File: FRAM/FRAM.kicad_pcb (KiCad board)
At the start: 2 copper layers, 50 x 31 mm, 8 parts, among them IC1 MB85RC256VPF-G-JNERE2, IC2 MB85RC256VPF-G-JNERE2, IC3 MB85RC256VPF-G-JNERE2, IC4 MB85RC256VPF-G-JNERE2

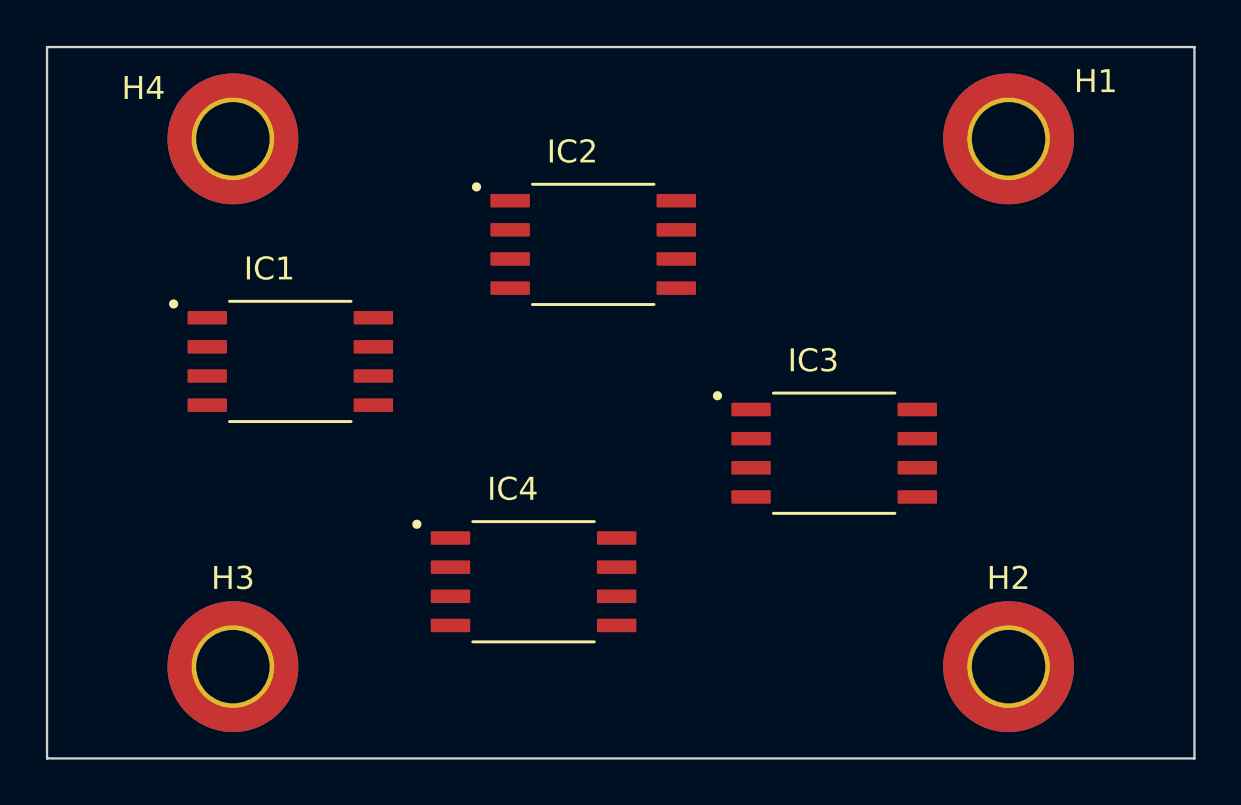
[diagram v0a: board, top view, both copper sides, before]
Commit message: Route sensors, IMU and radio board
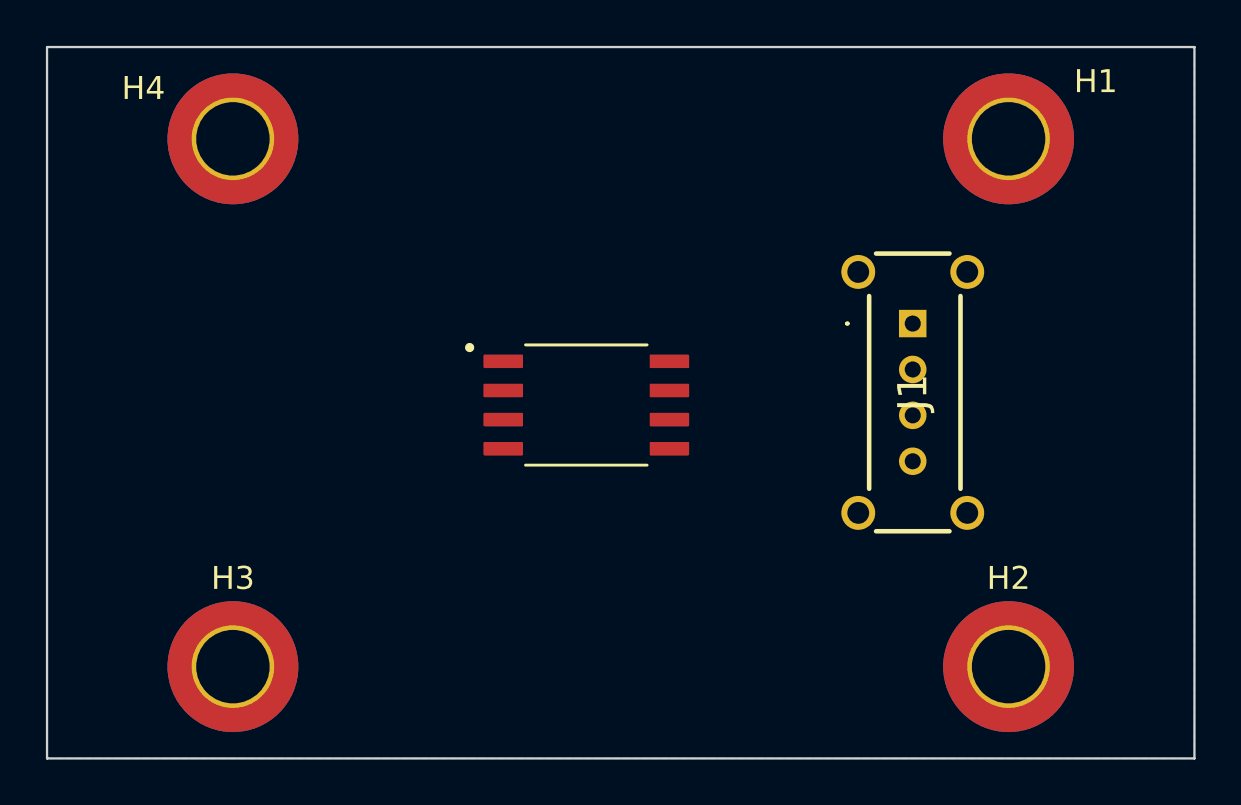
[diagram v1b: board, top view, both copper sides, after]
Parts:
- removed IC2, IC3, IC4: MB85RC256VPF-G-JNERE2, MB85RC256VPF-G-JNERE2:SOP127P797X210-8N
- added J1: M80-8770405, KiCad:M808770405, F.Cu at (135.7, 89.8)
- moved IC1 13.0 mm to (121.5, 93.4)
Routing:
- added copper zone on B.Cu, net GND

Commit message: Done with most of the boards
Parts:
- added R1: R, Resistor_SMD:R_0603_1608Metric, F.Cu at (127.7, 84.1)
- added R2: R, Resistor_SMD:R_0603_1608Metric, F.Cu at (127.7, 86.6)
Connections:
- J1 pad 2: unconnected-(J1-Pad2) -> GND
- J1 pad 3: +3V3 -> /SCL
- J1 pad 4: +3V3 -> /SDA
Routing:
- net +3V3: track 0.00 -> 11.3 mm
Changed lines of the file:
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@@
   (net 5 "+3V3")
   (net 6 "/WP")
-  (net 7 "unconnected-(J1-Pad2)")
-  (net 8 "unconnected-(J1-PadMH1)")
-  (net 9 "unconnected-(J1-PadMH2)")
-  (net 10 "unconnected-(J1-PadMH3)")
-  (net 11 "unconnected-(J1-PadMH4)")
+  (net 7 "unconnected-(J1-PadMH1)")
+  (net 8 "unconnected-(J1-PadMH2)")
+  (net 9 "unconnected-(J1-PadMH3)")
+  (net 10 "unconnected-(J1-PadMH4)")
+  (net 11 "/SCL")
+  (net 12 "/SDA")
+  (net 13 "Net-(IC2-SCL)")
+  (footprint "Resistor_SMD:R_0603_1608Metric" (layer "F.Cu")
+    (at 127.675 86.6)
+    (descr "Resistor SMD 0603 (1608 Metric), square (rectangular) end terminal, IPC_7351 nominal, (Body size source: IPC-SM-782 page 72, https://www.pcb-3d.com/wordpress/wp-content/uploads/ipc-sm-782a_amendment_1_and_2.pdf), generated with kicad-footprint-generator")
+    (tags "resistor")
+    (property "Sheetfile" "FRAM.kicad_sch")
+    (property "Sheetname" "")
+    (property "ki_description" "Resistor")
+    (property "ki_keywords" "R res resistor")
+    (attr smd)
+    (fp_text reference "R2" (at 0 -1.43) (layer "F.SilkS")
+        (effects (font (size 1 1) (thickness 0.15)))
+    )
+    (fp_text value "R" (at 0 1.43) (layer "F.Fab")
+        (effects (font (size 1 1) (thickness 0.15)))
+    )
+    (fp_text user "${REFERENCE}" (at 0 0) (layer "F.Fab")
+        (effects (font (size 0.4 0.4) (thickness 0.06)))
+    )
+    (fp_line (start -0.237258 -0.5225) (end 0.237258 -0.5225)
+      (stroke (width 0.12) (type solid)) (layer "F.SilkS"))
+    (fp_line (start -0.237258 0.5225) (end 0.237258 0.5225)
+      (stroke (width 0.12) (type solid)) (layer "F.SilkS"))
+    (fp_line (start -1.48 -0.73) (end 1.48 -0.73)
+      (stroke (width 0.05) (type solid)) (layer "F.CrtYd"))
+    (fp_line (start -1.48 0.73) (end -1.48 -0.73)
+      (stroke (width 0.05) (type solid)) (layer "F.CrtYd"))
+    (fp_line (start 1.48 -0.73) (end 1.48 0.73)
+      (stroke (width 0.05) (type solid)) (layer "F.CrtYd"))
+    (fp_line (start 1.48 0.73) (end -1.48 0.73)
+      (stroke (width 0.05) (type solid)) (layer "F.CrtYd"))
+    (fp_line (start -0.8 -0.4125) (end 0.8 -0.4125)
+      (stroke (width 0.1) (type solid)) (layer "F.Fab"))
+    (fp_line (start -0.8 0.4125) (end -0.8 -0.4125)
+      (stroke (width 0.1) (type solid)) (layer "F.Fab"))
+    (fp_line (start 0.8 -0.4125) (end 0.8 0.4125)
+      (stroke (width 0.1) (type solid)) (layer "F.Fab"))
+    (fp_line (start 0.8 0.4125) (end -0.8 0.4125)
+      (stroke (width 0.1) (type solid)) (layer "F.Fab"))
+    (pad "1" smd roundrect (at -0.825 0) (size 0.8 0.95) (layers "F.Cu" "F.Paste" "F.Mask") (roundrect_rratio 0.25)
+      (net 12 "/SDA") (pintype "passive"))
+    (pad "2" smd roundrect (at 0.825 0) (size 0.8 0.95) (layers "F.Cu" "F.Paste" "F.Mask") (roundrect_rratio 0.25)
+      (net 12 "/SDA") (pintype "passive"))
+    (model "${KICAD6_3DMODEL_DIR}/Resistor_SMD.3dshapes/R_0603_1608Metric.wrl"
+      (offset (xyz 0 0 0))
+      (scale (xyz 1 1 1))
+      (rotate (xyz 0 0 0))
+    )
+  )
+  (footprint "Resistor_SMD:R_0603_1608Metric" (layer "F.Cu")
+    (at 127.675 84.09)
+    (descr "Resistor SMD 0603 (1608 Metric), square (rectangular) end terminal, IPC_7351 nominal, (Body size source: IPC-SM-782 page 72, https://www.pcb-3d.com/wordpress/wp-content/uploads/ipc-sm-782a_amendment_1_and_2.pdf), generated with kicad-footprint-generator")
+    (tags "resistor")
+    (property "Sheetfile" "FRAM.kicad_sch")
+    (property "Sheetname" "")
+    (property "ki_description" "Resistor")
+    (property "ki_keywords" "R res resistor")
+    (attr smd)
+    (fp_text reference "R1" (at 0 -1.43) (layer "F.SilkS")
+        (effects (font (size 1 1) (thickness 0.15)))
+    )
+    (fp_text value "R" (at 0 1.43) (layer "F.Fab")
+        (effects (font (size 1 1) (thickness 0.15)))
+    )
+    (fp_text user "${REFERENCE}" (at 0 0) (layer "F.Fab")
+        (effects (font (size 0.4 0.4) (thickness 0.06)))
+    )
+    (fp_line (start -0.237258 -0.5225) (end 0.237258 -0.5225)
+      (stroke (width 0.12) (type solid)) (layer "F.SilkS"))
+    (fp_line (start -0.237258 0.5225) (end 0.237258 0.5225)
+      (stroke (width 0.12) (type solid)) (layer "F.SilkS"))
+    (fp_line (start -1.48 -0.73) (end 1.48 -0.73)
+      (stroke (width 0.05) (type solid)) (layer "F.CrtYd"))
+    (fp_line (start -1.48 0.73) (end -1.48 -0.73)
+      (stroke (width 0.05) (type solid)) (layer "F.CrtYd"))
+    (fp_line (start 1.48 -0.73) (end 1.48 0.73)
+      (stroke (width 0.05) (type solid)) (layer "F.CrtYd"))
+    (fp_line (start 1.48 0.73) (end -1.48 0.73)
+      (stroke (width 0.05) (type solid)) (layer "F.CrtYd"))
+    (fp_line (start -0.8 -0.4125) (end 0.8 -0.4125)
+      (stroke (width 0.1) (type solid)) (layer "F.Fab"))
+    (fp_line (start -0.8 0.4125) (end -0.8 -0.4125)
+      (stroke (width 0.1) (type solid)) (layer "F.Fab"))
+    (fp_line (start 0.8 -0.4125) (end 0.8 0.4125)
+      (stroke (width 0.1) (type solid)) (layer "F.Fab"))
+    (fp_line (start 0.8 0.4125) (end -0.8 0.4125)
+      (stroke (width 0.1) (type solid)) (layer "F.Fab"))
+    (pad "1" smd roundrect (at -0.825 0) (size 0.8 0.95) (layers "F.Cu" "F.Paste" "F.Mask") (roundrect_rratio 0.25)
+      (net 13 "Net-(IC2-SCL)") (pintype "passive"))
+    (pad "2" smd roundrect (at 0.825 0) (size 0.8 0.95) (layers "F.Cu" "F.Paste" "F.Mask") (roundrect_rratio 0.25)
+      (net 11 "/SCL") (pintype "passive"))
+    (model "${KICAD6_3DMODEL_DIR}/Resistor_SMD.3dshapes/R_0603_1608Metric.wrl"
+      (offset (xyz 0 0 0))
+      (scale (xyz 1 1 1))
+      (rotate (xyz 0 0 0))
+    )
+  )
   (footprint "MountingHole:MountingHole_3.2mm_M3_ISO7380_Pad_TopBottom" (layer "F.Cu")
     (at 106.1 104.8)
@@
       (net 5 "+3V3") (pinfunction "1") (pintype "passive"))
     (pad "2" thru_hole circle (at -2 0 90) (size 1.2 1.2) (drill 0.7) (layers "*.Cu" "*.Mask")
-      (net 7 "unconnected-(J1-Pad2)") (pinfunction "2") (pintype "passive"))
+      (net 4 "GND") (pinfunction "2") (pintype "passive"))
     (pad "3" thru_hole circle (at -4 0 90) (size 1.2 1.2) (drill 0.7) (layers "*.Cu" "*.Mask")
-      (net 5 "+3V3") (pinfunction "3") (pintype "passive"))
+      (net 11 "/SCL") (pinfunction "3") (pintype "passive"))
     (pad "4" thru_hole circle (at -6 0 90) (size 1.2 1.2) (drill 0.7) (layers "*.Cu" "*.Mask")
-      (net 5 "+3V3") (pinfunction "4") (pintype "passive"))
+      (net 12 "/SDA") (pinfunction "4") (pintype "passive"))
     (pad "MH1" thru_hole circle (at 2.25 -2.375 90) (size 1.478 1.478) (drill 0.95) (layers "*.Cu" "*.Mask")
-      (net 8 "unconnected-(J1-PadMH1)") (pinfunction "MH1") (pintype "passive"))
+      (net 7 "unconnected-(J1-PadMH1)") (pinfunction "MH1") (pintype "passive+no_connect"))
     (pad "MH2" thru_hole circle (at 2.25 2.375 90) (size 1.478 1.478) (drill 0.95) (layers "*.Cu" "*.Mask")
-      (net 9 "unconnected-(J1-PadMH2)") (pinfunction "MH2") (pintype "passive"))
+      (net 8 "unconnected-(J1-PadMH2)") (pinfunction "MH2") (pintype "passive+no_connect"))
     (pad "MH3" thru_hole circle (at -8.25 2.375 90) (size 1.478 1.478) (drill 0.95) (layers "*.Cu" "*.Mask")
-      (net 10 "unconnected-(J1-PadMH3)") (pinfunction "MH3") (pintype "passive"))
+      (net 9 "unconnected-(J1-PadMH3)") (pinfunction "MH3") (pintype "passive+no_connect"))
     (pad "MH4" thru_hole circle (at -8.25 -2.375 90) (size 1.478 1.478) (drill 0.95) (layers "*.Cu" "*.Mask")
-      (net 11 "unconnected-(J1-PadMH4)") (pinfunction "MH4") (pintype "passive"))
+      (net 10 "unconnected-(J1-PadMH4)") (pinfunction "MH4") (pintype "passive+no_connect"))
     (model "M80-8770405.stp"
       (offset (xyz 0 0 0))
@@
   (gr_line (start 98 77.8) (end 98 108.8)
     (stroke (width 0.1) (type default)) (layer "Edge.Cuts"))
+  (segment (start 125.12 91.495) (end 126.765 89.85) (width 0.25) (layer "F.Cu") (net 5))
+  (segment (start 126.765 89.85) (end 135.725 89.85) (width 0.25) (layer "F.Cu") (net 5))
   (zone (net 4) (net_name "GND") (layer "B.Cu") (hatch edge 0.5)
     (connect_pads (clearance 0.5))

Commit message: LC24 PCBs
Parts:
- removed IC1: MB85RC256VPF-G-JNERE2, MB85RC256VPF-G-JNERE2:SOP127P797X210-8N
- removed J1: M80-8770405, KiCad:M808770405
- added IC2: MB85RC256VPF-G-JNERE2, FRAM:FPT-8P-M08_FUJ, F.Cu at (115.0, 92.5)
- added J2: M80-8770422, Harwin-M80-8770422:CONN_M80-87704_HRW, F.Cu at (132.5, 89.8)
- added JP1: SolderJumper_2_Open, Jumper:SolderJumper-2_P1.3mm_Open_RoundedPad1.0x1.5mm, F.Cu at (103.8, 89.0)
- added JP2: SolderJumper_2_Open, Jumper:SolderJumper-2_P1.3mm_Open_RoundedPad1.0x1.5mm, F.Cu at (103.8, 93.0)
- added JP3: SolderJumper_2_Open, Jumper:SolderJumper-2_P1.3mm_Open_RoundedPad1.0x1.5mm, F.Cu at (103.8, 97.0)
- H1, H2, H3, H4: footprint MountingHole:MountingHole_3.2mm_M3_ISO7380_Pad_TopBottom -> Mounting_Wuerth:Mounting_Wuerth_WA-SMSI-M1.6_H1mm_9774010633
- R1, R2: value R -> 10k; footprint Resistor_SMD:R_0603_1608Metric -> Resistor_SMD:R_0201_0603Metric_Pad0.64x0.40mm_HandSolder
- moved R1 11.0 mm to (124.0, 94.5), turned to 90 degrees
- moved R2 6.53 mm to (124.0, 92.0), turned to -90 degrees
- moved H3 4.51 mm to (101.9, 103.1)
- moved H4 4.35 mm to (101.9, 83.1)
- moved H2 2.68 mm to (141.9, 103.1)
- moved H1 2.40 mm to (141.9, 83.1)
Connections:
- H1 pad 1: (no net) -> GND
- H2 pad 1: (no net) -> GND
- H3 pad 1: (no net) -> GND
- H4 pad 1: (no net) -> GND
- R1 pad 1: Net-(IC2-SCL) -> +3.3V
- R1 pad 2: /SCL -> /SDA
- R2 pad 1: /SDA -> +3.3V
- R2 pad 2: /SDA -> /SCL
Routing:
- net +3.3V: track 0.00 -> 77.4 mm
- net /SCL: track 0.00 -> 14.4 mm
- net /SDA: track 0.00 -> 14.3 mm
- net +3V3: track 11.3 -> 0.00 mm
- net Net-(IC2-A2): track 0.00 -> 8.41 mm
- net Net-(IC2-A0): track 0.00 -> 7.46 mm
- net Net-(IC2-A1): track 0.00 -> 7.27 mm
- net GND: track 0.00 -> 7.20 mm, vias 0 -> 3
- added copper zone on F.Cu, net GND
- removed copper zone on B.Cu, net GND
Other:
- board text added: "GND"
- board text added: "SCL"
- board text added: "SDA"
- board text added: "VDD"
